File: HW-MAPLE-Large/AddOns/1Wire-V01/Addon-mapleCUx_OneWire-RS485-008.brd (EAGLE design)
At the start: 67 x 47 mm, 39 parts, among them IC1 DS2482, IC31 ATMEGA168-TQFP, Q1 BSS84, X31 M03X2, X4 1751248, X7 1751264, Y2 8MHZ

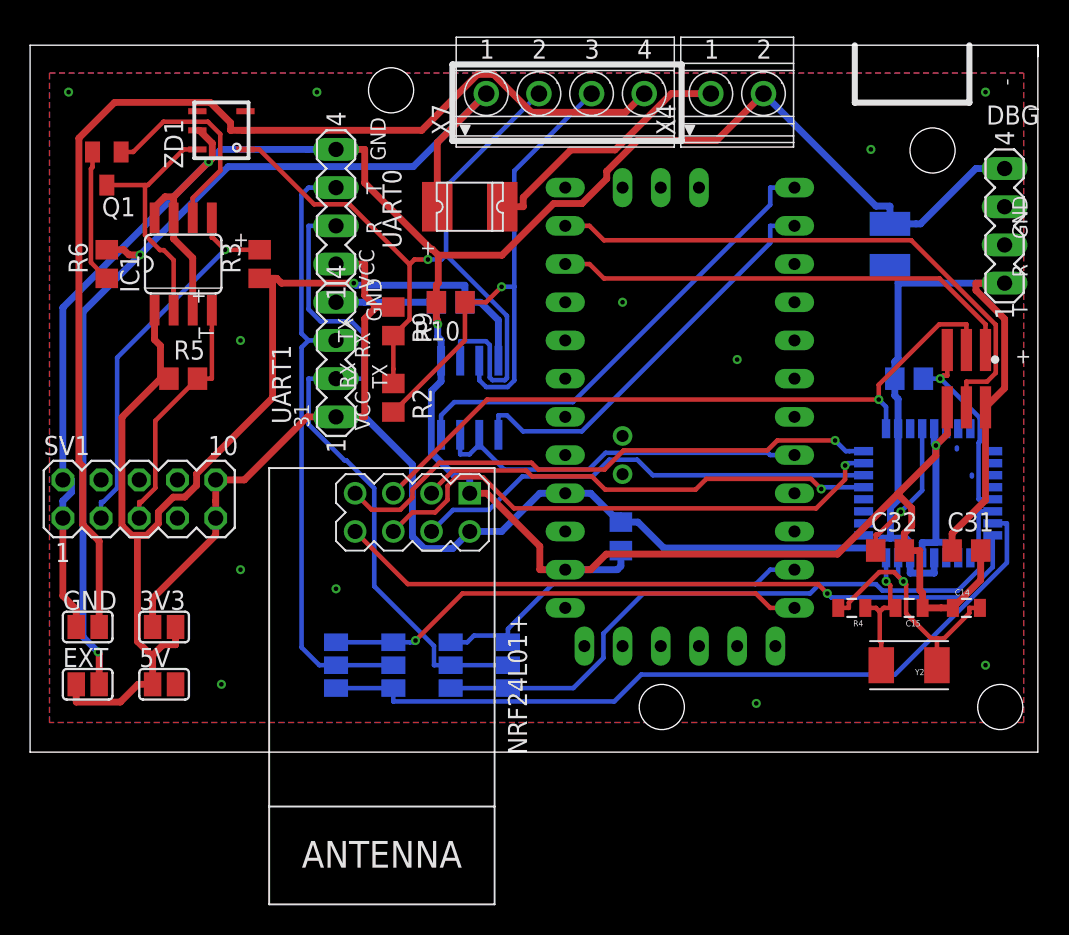
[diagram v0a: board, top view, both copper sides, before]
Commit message: Update RFM95, etc.
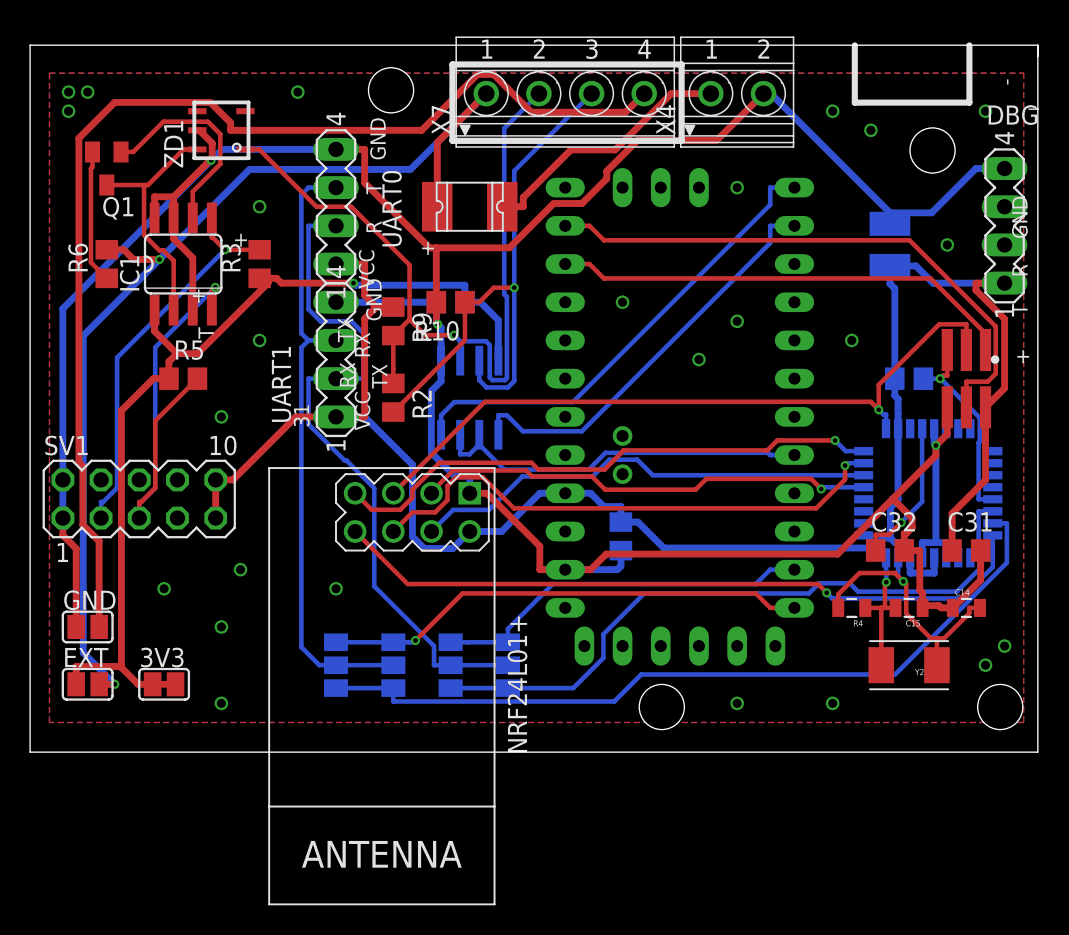
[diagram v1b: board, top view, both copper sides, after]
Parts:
- removed 5V: (no value), jumper:SJ
- moved 3V3 3.81 mm to (41.9, 16.5)
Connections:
- removed net +5V: 5V.2
- net VCC: no longer 3V3.1
- net VDD: now also 3V3.1; no longer 5V.1
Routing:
- net VDD: track 79.5 -> 63.5 mm
- net CC_IN_2: track 16.5 -> 30.1 mm, vias 0 -> 1
- net VCC: track 137.9 -> 129.8 mm
- net 1W: track 55.1 -> 53.1 mm
- net EXT: track 69.2 -> 71.2 mm
- net GND: track 219.2 -> 218.2 mm, vias 15 -> 28
